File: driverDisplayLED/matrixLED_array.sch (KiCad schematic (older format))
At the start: 28 parts, among them J10 Conn_01x12_Male, J11 Conn_01x12_Male, J12 Conn_01x12_Male, J13 Conn_01x12_Male, J14 Conn_01x12_Male, J15 Conn_01x12_Male, J16 Conn_01x12_Male, J17 Conn_01x12_Male, J2 Conn_01x12_Male, J3 Conn_01x12_Male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

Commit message: Agrego codigos de catalogo, documentación, y linkeo del borrador del PCB
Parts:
- L1, L3: CodigoCatalogo (none) -> 6970622931652; Field5 (none) -> https://opencircuit.shop/Product/LED-Matrix-white-8x8-modul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
- L2, L4, L5, L7, L8: CodigoCatalogo (none) -> 6970622931652
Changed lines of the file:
@@
 F 2 "myLedMatrixFootprint:1588AB-24" H 1655 2960 50  0001 C CNN
 F 3 "https://www.google.com/url?sa=t&rct=j&q=&esrc=s&source=web&cd=&ved=2ahUKEwiy--_K0qzsAhXCGbkGHUJoA-YQFjAFegQICRAC&url=http%3A%2F%2Fwww.ledtoplite.com%2Fuploadfile%2F2017%2F1588%2FTOP-CC-1588AB.pdf&usg=AOvVaw39C9W6BYCpxevXqqjI7nQH" H 1655 2960 50  0001 C CNN
+F 4 "6970622931652" H 1565 2515 50  0001 C CNN "CodigoCatalogo"
+F 5 "https://opencircuit.shop/Product/LED-Matrix-white-8x8-module-32x32mm-MAX7219" H 1565 2515 50  0001 C CNN "Field5"
 	1    1565 2515
 	1    0    0    -1
@@
 F 2 "myLedMatrixFootprint:1588AB-24" H 3425 2960 50  0001 C CNN
 F 3 "https://www.google.com/url?sa=t&rct=j&q=&esrc=s&source=web&cd=&ved=2ahUKEwiy--_K0qzsAhXCGbkGHUJoA-YQFjAFegQICRAC&url=http%3A%2F%2Fwww.ledtoplite.com%2Fuploadfile%2F2017%2F1588%2FTOP-CC-1588AB.pdf&usg=AOvVaw39C9W6BYCpxevXqqjI7nQH" H 3425 2960 50  0001 C CNN
+F 4 "6970622931652" H 3335 2515 50  0001 C CNN "CodigoCatalogo"
+F 5 "https://opencircuit.shop/Product/LED-Matrix-white-8x8-module-32x32mm-MAX7219" H 3335 2515 50  0001 C CNN "Field5"
 	1    3335 2515
 	1    0    0    -1
@@
 F 2 "myLedMatrixFootprint:1588AB-24" H 5225 2960 50  0001 C CNN
 F 3 "https://www.google.com/url?sa=t&rct=j&q=&esrc=s&source=web&cd=&ved=2ahUKEwiy--_K0qzsAhXCGbkGHUJoA-YQFjAFegQICRAC&url=http%3A%2F%2Fwww.ledtoplite.com%2Fuploadfile%2F2017%2F1588%2FTOP-CC-1588AB.pdf&usg=AOvVaw39C9W6BYCpxevXqqjI7nQH" H 5225 2960 50  0001 C CNN
+F 4 "6970622931652" H 5135 2515 50  0001 C CNN "CodigoCatalogo"
 	1    5135 2515
 	1    0    0    -1
@@
 F 2 "myLedMatrixFootprint:1588AB-24" H 6955 2960 50  0001 C CNN
 F 3 "https://www.google.com/url?sa=t&rct=j&q=&esrc=s&source=web&cd=&ved=2ahUKEwiy--_K0qzsAhXCGbkGHUJoA-YQFjAFegQICRAC&url=http%3A%2F%2Fwww.ledtoplite.com%2Fuploadfile%2F2017%2F1588%2FTOP-CC-1588AB.pdf&usg=AOvVaw39C9W6BYCpxevXqqjI7nQH" H 6955 2960 50  0001 C CNN
+F 4 "6970622931652" H 6865 2515 50  0001 C CNN "CodigoCatalogo"
 	1    6865 2515
 	1    0    0    -1
@@
 F 2 "myLedMatrixFootprint:1588AB-24" H 1665 5520 50  0001 C CNN
 F 3 "https://www.google.com/url?sa=t&rct=j&q=&esrc=s&source=web&cd=&ved=2ahUKEwiy--_K0qzsAhXCGbkGHUJoA-YQFjAFegQICRAC&url=http%3A%2F%2Fwww.ledtoplite.com%2Fuploadfile%2F2017%2F1588%2FTOP-CC-1588AB.pdf&usg=AOvVaw39C9W6BYCpxevXqqjI7nQH" H 1665 5520 50  0001 C CNN
+F 4 "6970622931652" H 1575 5075 50  0001 C CNN "CodigoCatalogo"
 	1    1575 5075
 	1    0    0    -1
@@
 F 2 "myLedMatrixFootprint:1588AB-24" H 3435 5520 50  0001 C CNN
 F 3 "https://www.google.com/url?sa=t&rct=j&q=&esrc=s&source=web&cd=&ved=2ahUKEwiy--_K0qzsAhXCGbkGHUJoA-YQFjAFegQICRAC&url=http%3A%2F%2Fwww.ledtoplite.com%2Fuploadfile%2F2017%2F1588%2FTOP-CC-1588AB.pdf&usg=AOvVaw39C9W6BYCpxevXqqjI7nQH" H 3435 5520 50  0001 C CNN
+F 4 "6970622931652" H 3345 5075 50  0001 C CNN "CodigoCatalogo"
 	1    3345 5075
 	1    0    0    -1
@@
 F 2 "myLedMatrixFootprint:1588AB-24" H 6955 5520 50  0001 C CNN
 F 3 "https://www.google.com/url?sa=t&rct=j&q=&esrc=s&source=web&cd=&ved=2ahUKEwiy--_K0qzsAhXCGbkGHUJoA-YQFjAFegQICRAC&url=http%3A%2F%2Fwww.ledtoplite.com%2Fuploadfile%2F2017%2F1588%2FTOP-CC-1588AB.pdf&usg=AOvVaw39C9W6BYCpxevXqqjI7nQH" H 6955 5520 50  0001 C CNN
+F 4 "6970622931652" H 6865 5075 50  0001 C CNN "CodigoCatalogo"
 	1    6865 5075
 	1    0    0    -1
@@
 Text Label 1990 5820 3    50   ~ 0
 Hb5
-Wire Bus Line
-	890  1650 890  6540
-Wire Bus Line
-	6160 1650 6160 6540
-Wire Bus Line
-	4440 1650 4440 6540
-Wire Bus Line
-	2630 1650 2630 6550
-Wire Bus Line
-	2530 4010 9490 4010
-Wire Bus Line
-	2530 1450 9490 1450
-Wire Bus Line
-	7380 4110 7730 4110
-Wire Bus Line
-	7380 6050 7710 6050
-Wire Bus Line
-	5650 4110 6000 4110
-Wire Bus Line
-	5660 6050 5990 6050
-Wire Bus Line
-	3850 4110 4200 4110
-Wire Bus Line
-	3860 6050 4190 6050
-Wire Bus Line
-	2080 4110 2430 4110
-Wire Bus Line
-	2090 6050 2420 6050
-Wire Bus Line
-	7375 1550 7730 1550
-Wire Bus Line
-	7380 3490 7710 3490
-Wire Bus Line
-	5625 1550 5980 1550
-Wire Bus Line
-	5650 3490 5980 3490
-Wire Bus Line
-	3850 1550 4200 1550
-Wire Bus Line
-	3850 3490 4180 3490
-Wire Bus Line
-	2075 1550 2430 1550
-Wire Bus Line
-	2080 3490 2410 3490
-Wire Bus Line
-	8440 1550 8440 2080
-Wire Bus Line
-	8445 3095 8445 3485
-Wire Bus Line
-	8440 5640 8440 6045
-Wire Bus Line
-	8440 4110 8440 4585
-Wire Bus Line
-	6260 4110 7280 4110
-Wire Bus Line
-	6450 6050 7280 6050
-Wire Bus Line
-	4540 4110 5560 4110
-Wire Bus Line
-	4730 6050 5560 6050
-Wire Bus Line
-	2730 4110 3770 4110
-Wire Bus Line
-	2930 6050 3760 6050
-Wire Bus Line
-	990  4110 1990 4110
-Wire Bus Line
-	1140 6050 1990 6050
-Wire Bus Line
-	6260 1550 7280 1550
-Wire Bus Line
-	6450 3490 7280 3490
-Wire Bus Line
-	4540 1550 5580 1550
-Wire Bus Line
-	4720 3490 5550 3490
-Wire Bus Line
-	2730 1550 3750 1550
-Wire Bus Line
-	2930 3490 3750 3490
-Wire Bus Line
-	990  1550 2010 1550
-Wire Bus Line
-	1140 3490 1980 3490
-Wire Bus Line
-	10135 2405 10135 3810
-Wire Bus Line
-	10135 3810 10135 5630
-Wire Bus Line
-	10615 2405 10615 6370
 Text HLabel 9490 6270 2    50   BiDi ~ 0
 Hb[5..8]
@@
 Text Label 9050 6270 0    50   ~ 0
 Hb[5..8]
+Wire Bus Line
+	890  1650 890  6540
+Wire Bus Line
+	6160 1650 6160 6540
+Wire Bus Line
+	4440 1650 4440 6540
+Wire Bus Line
+	2630 1650 2630 6550
+Wire Bus Line
+	2530 4010 9490 4010
+Wire Bus Line
+	2530 1450 9490 1450
+Wire Bus Line
+	7380 4110 7730 4110
+Wire Bus Line
+	7380 6050 7710 6050
+Wire Bus Line
+	5650 4110 6000 4110
+Wire Bus Line
+	5660 6050 5990 6050
+Wire Bus Line
+	3850 4110 4200 4110
+Wire Bus Line
+	3860 6050 4190 6050
+Wire Bus Line
+	2080 4110 2430 4110
+Wire Bus Line
+	2090 6050 2420 6050
+Wire Bus Line
+	7375 1550 7730 1550
+Wire Bus Line
+	7380 3490 7710 3490
+Wire Bus Line
+	5625 1550 5980 1550
+Wire Bus Line
+	5650 3490 5980 3490
+Wire Bus Line
+	3850 1550 4200 1550
+Wire Bus Line
+	3850 3490 4180 3490
+Wire Bus Line
+	2075 1550 2430 1550
+Wire Bus Line
+	2080 3490 2410 3490
+Wire Bus Line
+	8440 1550 8440 2080
+Wire Bus Line
+	8445 3095 8445 3485
+Wire Bus Line
+	8440 5640 8440 6045
+Wire Bus Line
+	8440 4110 8440 4585
+Wire Bus Line
+	6260 4110 7280 4110
+Wire Bus Line
+	6450 6050 7280 6050
+Wire Bus Line
+	4540 4110 5560 4110
+Wire Bus Line
+	4730 6050 5560 6050
+Wire Bus Line
+	2730 4110 3770 4110
+Wire Bus Line
+	2930 6050 3760 6050
+Wire Bus Line
+	990  4110 1990 4110
+Wire Bus Line
+	1140 6050 1990 6050
+Wire Bus Line
+	6260 1550 7280 1550
+Wire Bus Line
+	6450 3490 7280 3490
+Wire Bus Line
+	4540 1550 5580 1550
+Wire Bus Line
+	4720 3490 5550 3490
+Wire Bus Line
+	2730 1550 3750 1550
+Wire Bus Line
+	2930 3490 3750 3490
+Wire Bus Line
+	990  1550 2010 1550
+Wire Bus Line
+	1140 3490 1980 3490
+Wire Bus Line
+	10135 2405 10135 3810
+Wire Bus Line
+	10135 3810 10135 5630
+Wire Bus Line
+	10615 2405 10615 6370
 $EndSCHEMATC

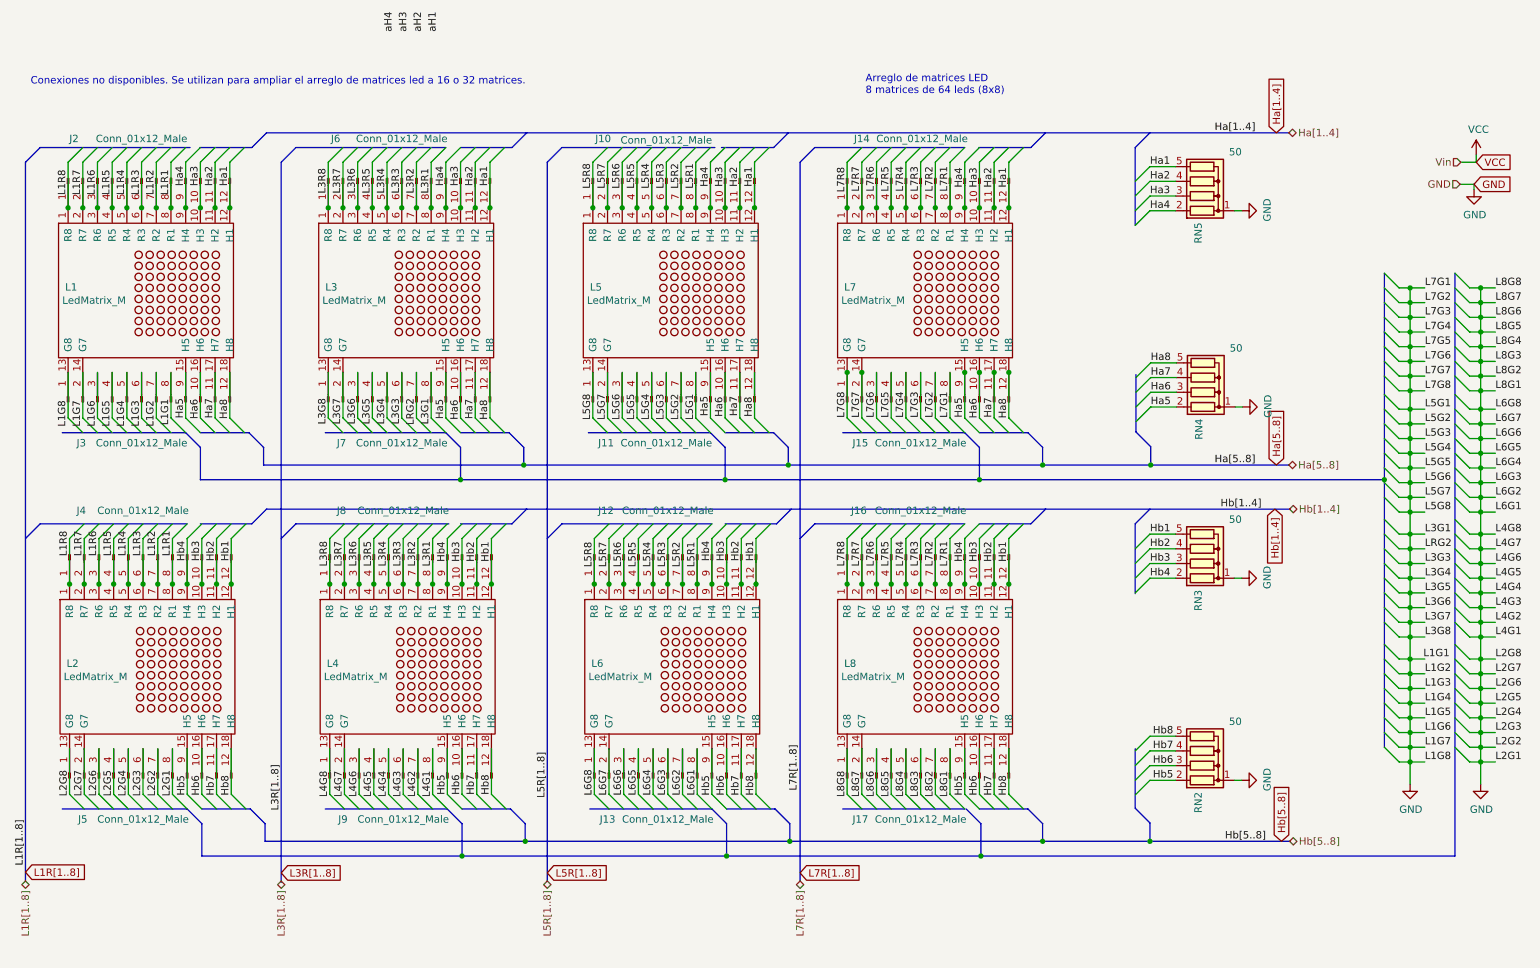
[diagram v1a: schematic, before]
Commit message: Agrego nuevo proyecto: Modulo Infrarrojo TxRx
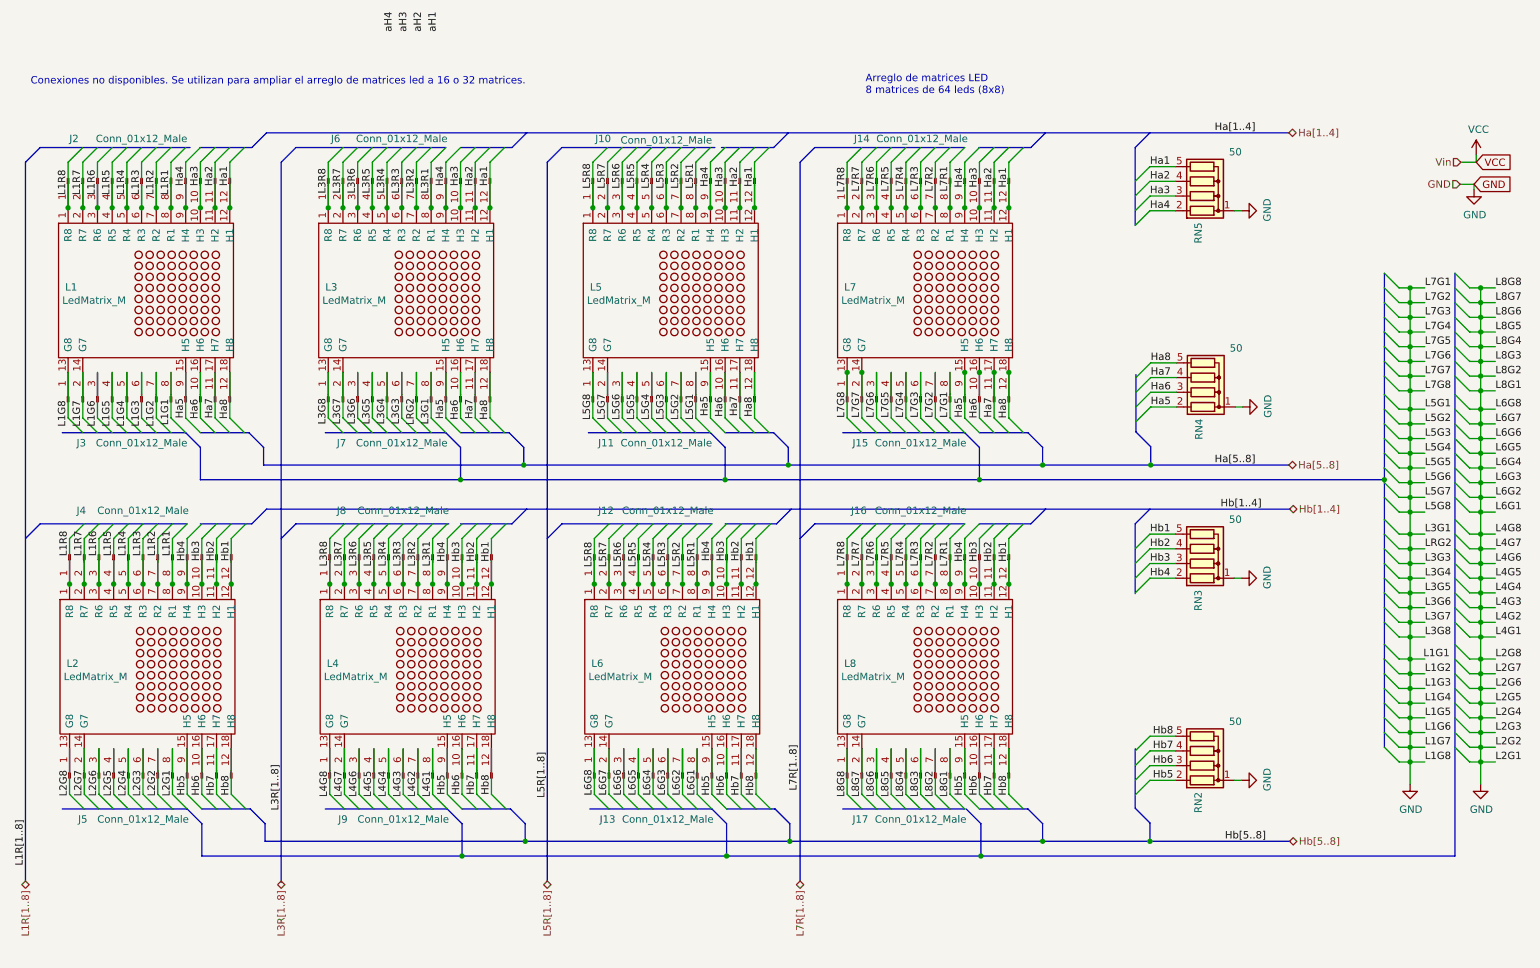
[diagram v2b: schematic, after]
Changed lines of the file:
@@
 Text Label 890  6435 1    50   ~ 0
-L1R[1..8]
-Text GLabel 890  6480 2    50   Input ~ 0
 L1R[1..8]
 Text Label 2630 6060 1    50   ~ 0
@@
 L5R[1..8]
 Text Label 6155 5925 1    50   ~ 0
-L7R[1..8]
-Text GLabel 2630 6485 2    50   Input ~ 0
-L3R[1..8]
-Text GLabel 4440 6485 2    50   Input ~ 0
-L5R[1..8]
-Text GLabel 6160 6485 2    50   Input ~ 0
 L7R[1..8]
 Text Label 3400 625  3    50   ~ 0
@@
 Text Label 7280 1685 3    50   ~ 0
 Ha4
-Text GLabel 9400 1450 1    50   Input ~ 0
-Ha[1..4]
 Text HLabel 9485 3710 2    50   BiDi ~ 0
 Ha[5..8]
 Text Label 8980 3710 0    50   ~ 0
-Ha[5..8]
-Text GLabel 9400 3710 1    50   Input ~ 0
 Ha[5..8]
 Text Label 5550 3240 3    50   ~ 0
@@
 Text Label 9020 4010 0    50   ~ 0
 Hb[1..4]
-Text GLabel 9390 4010 3    50   Input ~ 0
-Hb[1..4]
 Text Label 8560 5555 0    50   ~ 0
 Hb8
@@
 Text HLabel 9490 6270 2    50   BiDi ~ 0
 Hb[5..8]
-Text GLabel 9435 6270 1    50   Input ~ 0
-Hb[5..8]
 Text Label 9050 6270 0    50   ~ 0
